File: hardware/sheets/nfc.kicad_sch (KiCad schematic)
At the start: 0 parts

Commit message: hw: draw UI, IMU, microphone and NFC sheets
IMU: ICM-42688-P on the shared I2C1 bus at 0x68, bypassed as TDK's
application circuit specifies, reserved pins to ground, and unfitted
links for the SPI fallback.

Microphone: SPH0641LM4H-1 with a C0G bypass capacitor (Knowles advises
against class 2 dielectrics next to the part), a 0 ohm supply link for
current measurement, series options on clock and data, and SELECT to
ground.

NFC: NT3H2111W0FHKH powered from the NFC_PWR GPIO with its bus and
field-detect pull-ups, the PCB coil as a non-BOM part, two unfitted
tuning capacitor positions and test points for bus timing.

UI: two tact switches to ground with unfitted external pull-ups and a
red status LED.

The labels these sheets connect no longer need ERC exclusions. NFC_PWR
gets a reviewed exclusion: a GPIO drives the tag supply by design.
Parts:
- added C1101: 100nF, Capacitor_SMD:C_0402_1005Metric, symbol Device:C
- added C1102, C1103: DNP, Capacitor_SMD:C_0402_1005Metric, symbol Device:C
- added L1101: NFC coil 30x25mm 6T (PCB), symbol Device:L
- added R1101, R1102: 4.7k, Resistor_SMD:R_0402_1005Metric, symbol Device:R
- added R1103: 10k, Resistor_SMD:R_0402_1005Metric, symbol Device:R
- added R1104: DNP, Resistor_SMD:R_0402_1005Metric, symbol Device:R
- added TP1101: NFC_PWR, TestPoint:TestPoint_Pad_D1.0mm, symbol Connector:TestPoint
- added TP1102: NFC_SDA, TestPoint:TestPoint_Pad_D1.0mm, symbol Connector:TestPoint
- added TP1103: NFC_SCL, TestPoint:TestPoint_Pad_D1.0mm, symbol Connector:TestPoint
- added TP1104: NFC_FD, TestPoint:TestPoint_Pad_D1.0mm, symbol Connector:TestPoint
- added U1101: NT3H2111W0FHKH, smart-led-badge:NXP_XQFN-8_SOT902-3, symbol smart-led-badge:NT3H2111W0FHKH
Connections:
- new net +3V3: R1104.1
- new net GND: C1101.2, U1101.2 (VSS)
- new net NFC_FD: R1103.1, TP1104.1, U1101.4 (FD)
- new net NFC_LA: C1102.1, C1103.1, L1101.1, U1101.1 (LA)
- new net NFC_LB: C1102.2, C1103.2, L1101.2, U1101.8 (LB)
- new net NFC_PWR: C1101.1, R1101.2, R1102.2, R1103.2, R1104.2, TP1101.1, U1101.6 (VCC)
- new net NFC_SCL: R1101.1, TP1103.1, U1101.3 (SCL)
- new net NFC_SDA: R1102.1, TP1102.1, U1101.5 (SDA)
- no-connect marks 0 -> 1
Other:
- note added: "NFC (Rev A) - design notes NXP NT3H2111W0FHKH (Rev. 3.6; errata Rev. 4.1) on its own I2C bus (TWIM2, 100 kHz). VCC, bus and FD pull-ups come from the NFC_PWR GPIO (P1.10), on only during updates; RF reads are passive. VOUT (energy harvesting) unused. Coil: 30 x 25 mm, 6 turns, 0.4/0.3 mm, F.Cu with one In1.Cu crossover; no copper inside the coil region; battery and magnets outside it (DEC-008). R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"

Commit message: hw: apply layout footprint and test-point changes to the schematic
The matrix LEDs use the KENTO-pattern footprint, L1101 the PCB coil,
MK1001 the 0.6 mm hole footprint and J301 the project HRO copy.

Removes test points that duplicate others: TP303 and TP304, TP208 and
TP506, and TP501-TP503, whose signals are on the SWD header. Also
removes H1304, which the carrier does not use. Rail and GND test points
move to 0.8 mm pads.

nRESET now connects only the header's open-collector pin and the module
input. ERC reports that as not driven, so the error is excluded: the
nRF5340 has an internal pull-up on reset.
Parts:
- L1101: footprint (none) -> smart-led-badge:L_NFC_Coil_30x25mm_6T
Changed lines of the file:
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@@
 		(in_bom no)
 		(on_board yes)
-		(in_pos_files yes)
+		(in_pos_files no)
 		(dnp no)
 		(property "Reference" "L1101"
@@
 			)
 		)
-		(property "Footprint" ""
+		(property "Footprint" "smart-led-badge:L_NFC_Coil_30x25mm_6T"
 			(at 50.8 88.9 0)
 			(hide yes)

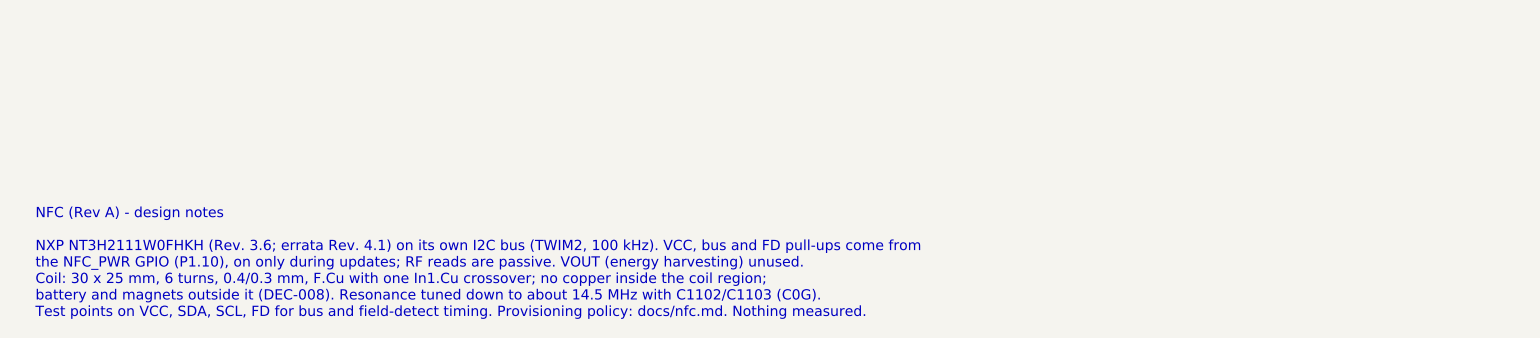
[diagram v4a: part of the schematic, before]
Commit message: hw: replace the MDBT53 with the E73 nRF52840 module (#23)
* hw: add E73-2G4M08S1C library assets

Add the symbol, footprint and envelope model for the Ebyte
E73-2G4M08S1C (nRF52840) module that replaces the MDBT53-P1M on Rev A.

The footprint follows the Ebyte specification drawing, mirrored from
the bottom view, and every pad centre was checked against the drawing
dimensions. Castellated lands extend 0.3 mm beyond the body. Ebyte
publishes no antenna keep-out, so the footprint keeps every copper
layer clear at the ceramic-antenna end. The symbol reuses the MDBT53
pin locations per net so the MCU sheet wiring carries over. The 3D
model is a 13 x 18 x 3.0 mm envelope for clearance checks only.

* hw: switch U401 to the E73 nRF52840 module

The MDBT53-P1M cannot be sourced in time for the Rev A order, while
the E73-2G4M08S1C is stocked at JLCPCB (ADR 0015).

The E73 holds its DC/DC inductors and decoupling, so L401/L402 and
C403/C404 are removed. The nRF52840 has no internal 32.768 kHz load,
so C405/C406 are fitted with 12 pF; the value is calculated and still
needs checking against the Product Specification. All 29 module GPIO
are used: CHG_STAT is no longer read by the MCU, and the UART pads,
spare GPIO pads and IMU SPI-fallback links are removed. Pins Ebyte
marks as low-frequency carry only analog inputs or slow signals.

* hw: place the E73 module in the bottom-right corner

The 13 x 18 mm module has its antenna end toward the bottom edge,
inset 0.9 mm so the body clears the 3 mm corner radius. USB-C moves
2.05 mm left to clear the module lands and antenna keep-out.

The crystal, its load capacitors, the supply capacitor and the USB
links sit at the pins they serve. The right column had no room for
every displaced part: U708 moves next to the column drivers whose
blanking it drives, Q302 moves to the bottom strip, and several test
points move further from their nets. The module area is not routed.

* docs: record the move to the nRF52840 module

Add ADR 0015 for t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
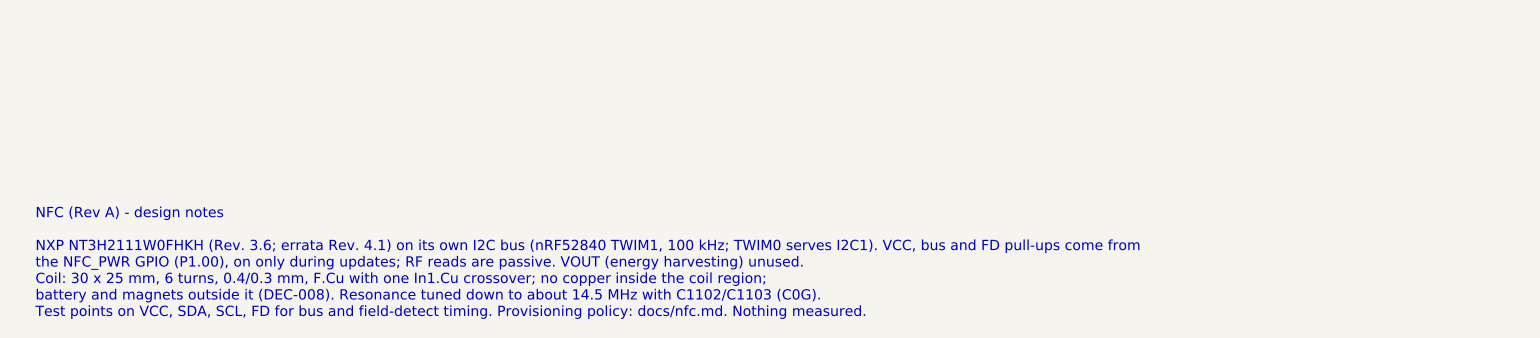
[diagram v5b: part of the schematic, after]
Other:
- note added: "NFC (Rev A) - design notes NXP NT3H2111W0FHKH (Rev. 3.6; errata Rev. 4.1) on its own I2C bus (nRF52840 TWIM1, 100 kHz; TWIM0 serves I2C1). VCC, bus and FD pull-ups come from the NFC_PWR GPIO (P1.00), on only during updates; RF reads are passive. VOUT (energy harvesting) unused. Coil: 30 x 25 mm, 6 turns, 0.4/0.3 mm, F.Cu with one In1.Cu crossover; no copper inside the coil region; battery and mag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"
- note removed: "NFC (Rev A) - design notes NXP NT3H2111W0FHKH (Rev. 3.6; errata Rev. 4.1) on its own I2C bus (TWIM2, 100 kHz). VCC, bus and FD pull-ups come from the NFC_PWR GPIO (P1.10), on only during updates; RF reads are passive. VOUT (energy harvesting) unused. Coil: 30 x 25 mm, 6 turns, 0.4/0.3 mm, F.Cu with one In1.Cu crossover; no copper inside the coil region; battery and magnets outside it (DEC-008). R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"
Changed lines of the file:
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@@
 		(comment 2 "Schematic frozen for layout after review 2026-10-07; not for fabrication until the release gate")
 	)
-	(text "NFC (Rev A) - design notes\n\nNXP NT3H2111W0FHKH (Rev. 3.6; errata Rev. 4.1) on its own I2C bus (TWIM2, 100 kHz). VCC, bus and FD pull-ups come from\nthe NFC_PWR GPIO (P1.10), on only during updates; RF reads are passive. VOUT (energy harvesting) unused.\nCoil: 30 x 25 mm, 6 turns, 0.4/0.3 mm, F.Cu with one In1.Cu crossover; no copper inside the coil region;\nbattery and magnets outside it (DEC-008). Resonance tuned down to about 14.5 MHz with C1102/C1103 (C0G).\nTest points on VCC, SDA, SCL, FD for bus and field-detect timing. Provisioning policy: docs/nfc.md. Nothing measured."
+	(text "NFC (Rev A) - design notes\n\nNXP NT3H2111W0FHKH (Rev. 3.6; errata Rev. 4.1) on its own I2C bus (nRF52840 TWIM1, 100 kHz; TWIM0 serves I2C1). VCC, bus and FD pull-ups come from\nthe NFC_PWR GPIO (P1.00), on only during updates; RF reads are passive. VOUT (energy harvesting) unused.\nCoil: 30 x 25 mm, 6 turns, 0.4/0.3 mm, F.Cu with one In1.Cu crossover; no copper inside the coil region;\nbattery and magnets outside it (DEC-008). Resonance tuned down to about 14.5 MHz with C1102/C1103 (C0G).\nTest points on VCC, SDA, SCL, FD for bus and field-detect timing. Provisioning policy: docs/nfc.md. Nothing measured."
 		(exclude_from_sim no)
 		(at 50.8 152.4 0)

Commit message: hw: lay out and route the Rev A board (#29)
* hw: add fab-layer references to custom footprints

Show each part's reference on F.Fab so the assembly drawing used for
bring-up and rework labels the custom parts the same way as the KiCad
library parts. Copper, courtyards and silkscreen are unchanged.

* hw: join the NFC coil's twin pad-2 ends as a jumper

The coil's inner and outer pad-2 ends are connected by footprint copper
(the In1 crossover), which KiCad does not count as a connection, so
NFC_LB stayed unrouted. Treat the duplicate pad numbers as a jumper.
The pad 1/2 net tie is unchanged.

* hw: remove unfitted parts and spare test points

Free routing room on the Rev A board:
- remove the eight DNP row pull-down arrays (RN709-RN716) and six DNP
  passive positions (C1103, R1005, R1104, R212, R213, R310)
- remove 19 test points outside the required set that had no room on
  the routed board

No net changes and no fitted-part changes, so the assembled board and
its BOM are the same. C1102 stays as the DNP NFC tuning position.

* hw: lay out and route the Rev A board

Place and route the 118 x 76 mm four-layer board: the 32 x 32 matrix at
45 degrees on the west, the row drivers in a column beside it, and the
power, charger, NFC, IMU, microphone and E73 module on the east. In1 is
a GND plane kept solid under the regulators, charger and module; a few
low-current signals cross it elsewhere where no other layer had room.
The board uses the JLC04161H-7628 stack-up, tented vias and
0.45/0.2 mm minimum vias.

Add release silkscreen: battery polarity at J302 on both faces,
test-point net names (front where they fit, rear behind each pad),
orientation-independent control marks, the board name and a designer
monogram on the NFC coil.

DRC and schematic parity are clean. Nothing is measured yet: charger,
USB, matrix timing, RF and NFC tuning remain bring-up checks. The README
and hardware docs now give the 118 x 76 mm outline.

* hw: move three vias out of component pads

The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
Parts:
- removed C1103: DNP, Capacitor_SMD:C_0402_1005Metric, symbol Device:C
- removed R1104: DNP, Resistor_SMD:R_0402_1005Metric, symbol Device:R
- removed TP1101: NFC_PWR, TestPoint:TestPoint_Pad_D1.0mm, symbol Connector:TestPoint
- removed TP1102: NFC_SDA, TestPoint:TestPoint_Pad_D1.0mm, symbol Connector:TestPoint
- removed TP1103: NFC_SCL, TestPoint:TestPoint_Pad_D1.0mm, symbol Connector:TestPoint
- removed TP1104: NFC_FD, TestPoint:TestPoint_Pad_D1.0mm, symbol Connector:TestPoint
